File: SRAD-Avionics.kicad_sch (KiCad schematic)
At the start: 3 parts, among them J1 Conn_01x02_Socket, U2 STM32H503RBTx, U3 MAX-8C

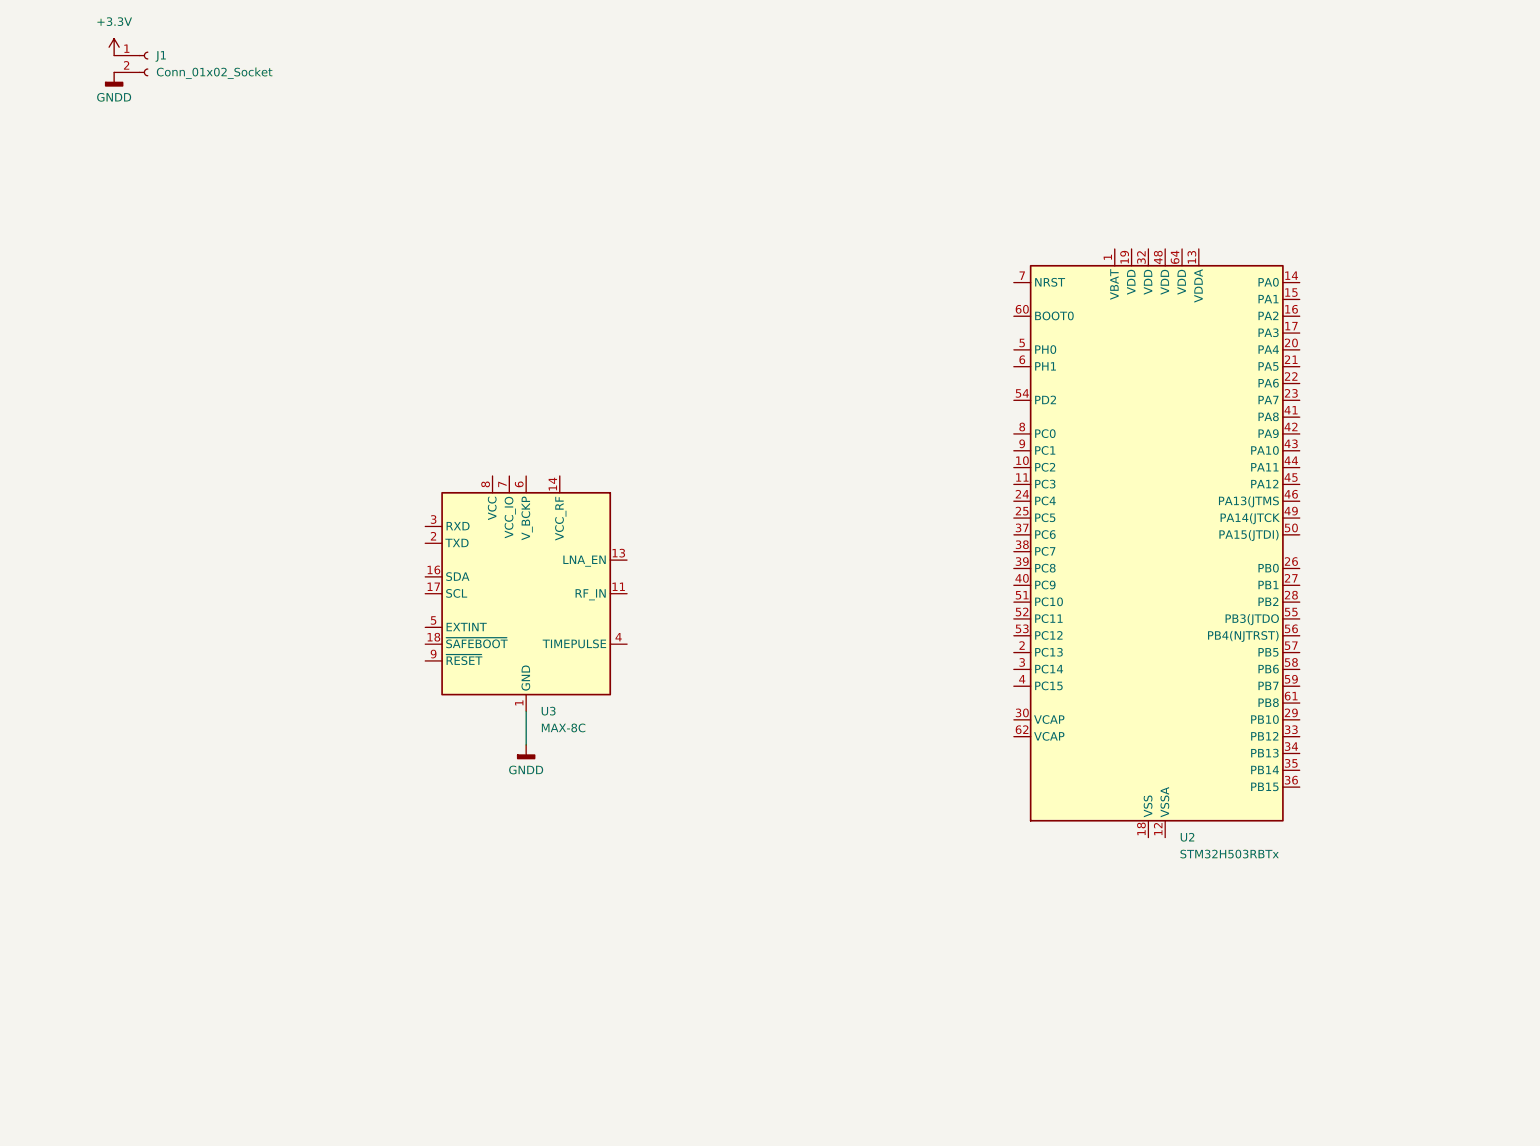
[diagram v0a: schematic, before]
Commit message: Finished schematics for battery charging and output voltage regulation
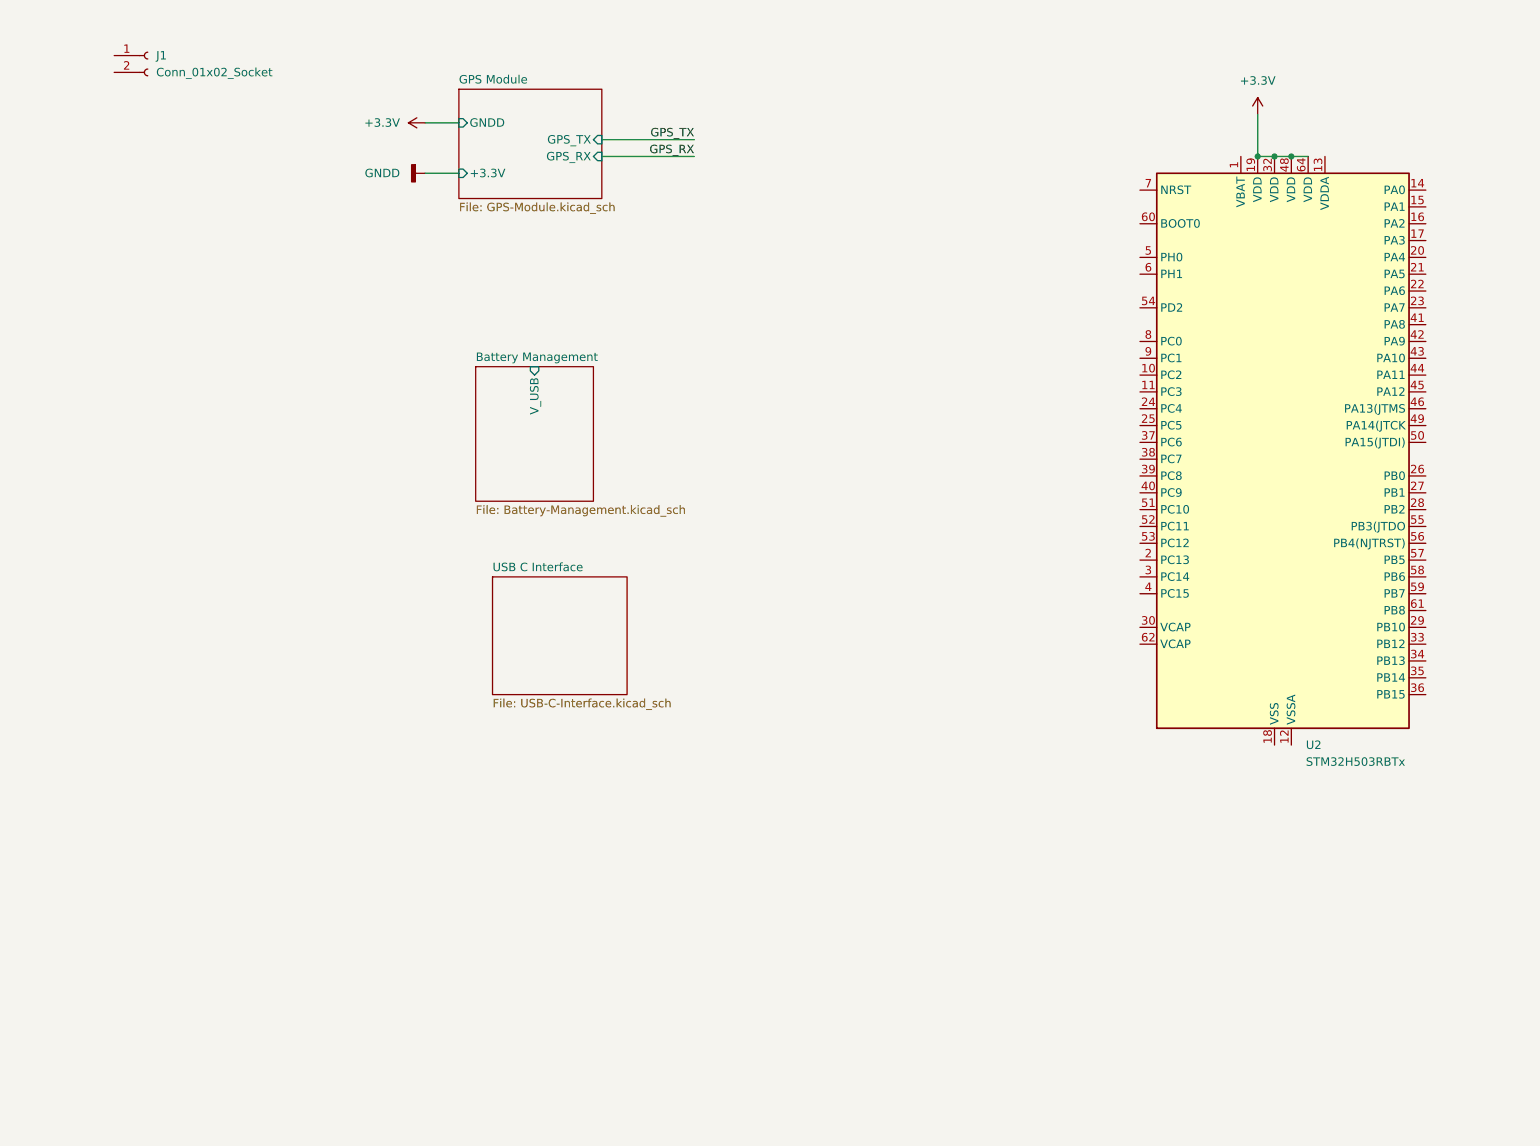
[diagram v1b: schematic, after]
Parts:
- removed U3: MAX-8C, RF_GPS:ublox_MAX, symbol RF_GPS:MAX-8C
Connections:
- net +3.3V: now also U2.19 (VDD), U2.32 (VDD), U2.48 (VDD), U2.64 (VDD); no longer J1.1 (Pin_1)
- net GNDD: no longer J1.2 (Pin_2)
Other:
- added sheet Battery Management (Battery-Management.kicad_sch)
- added sheet GPS Module (GPS-Module.kicad_sch)
- added sheet USB C Interface (USB-C-Interface.kicad_sch)
- moved on the sheet: U2

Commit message: Added USB C and CAN interfaces to schematic
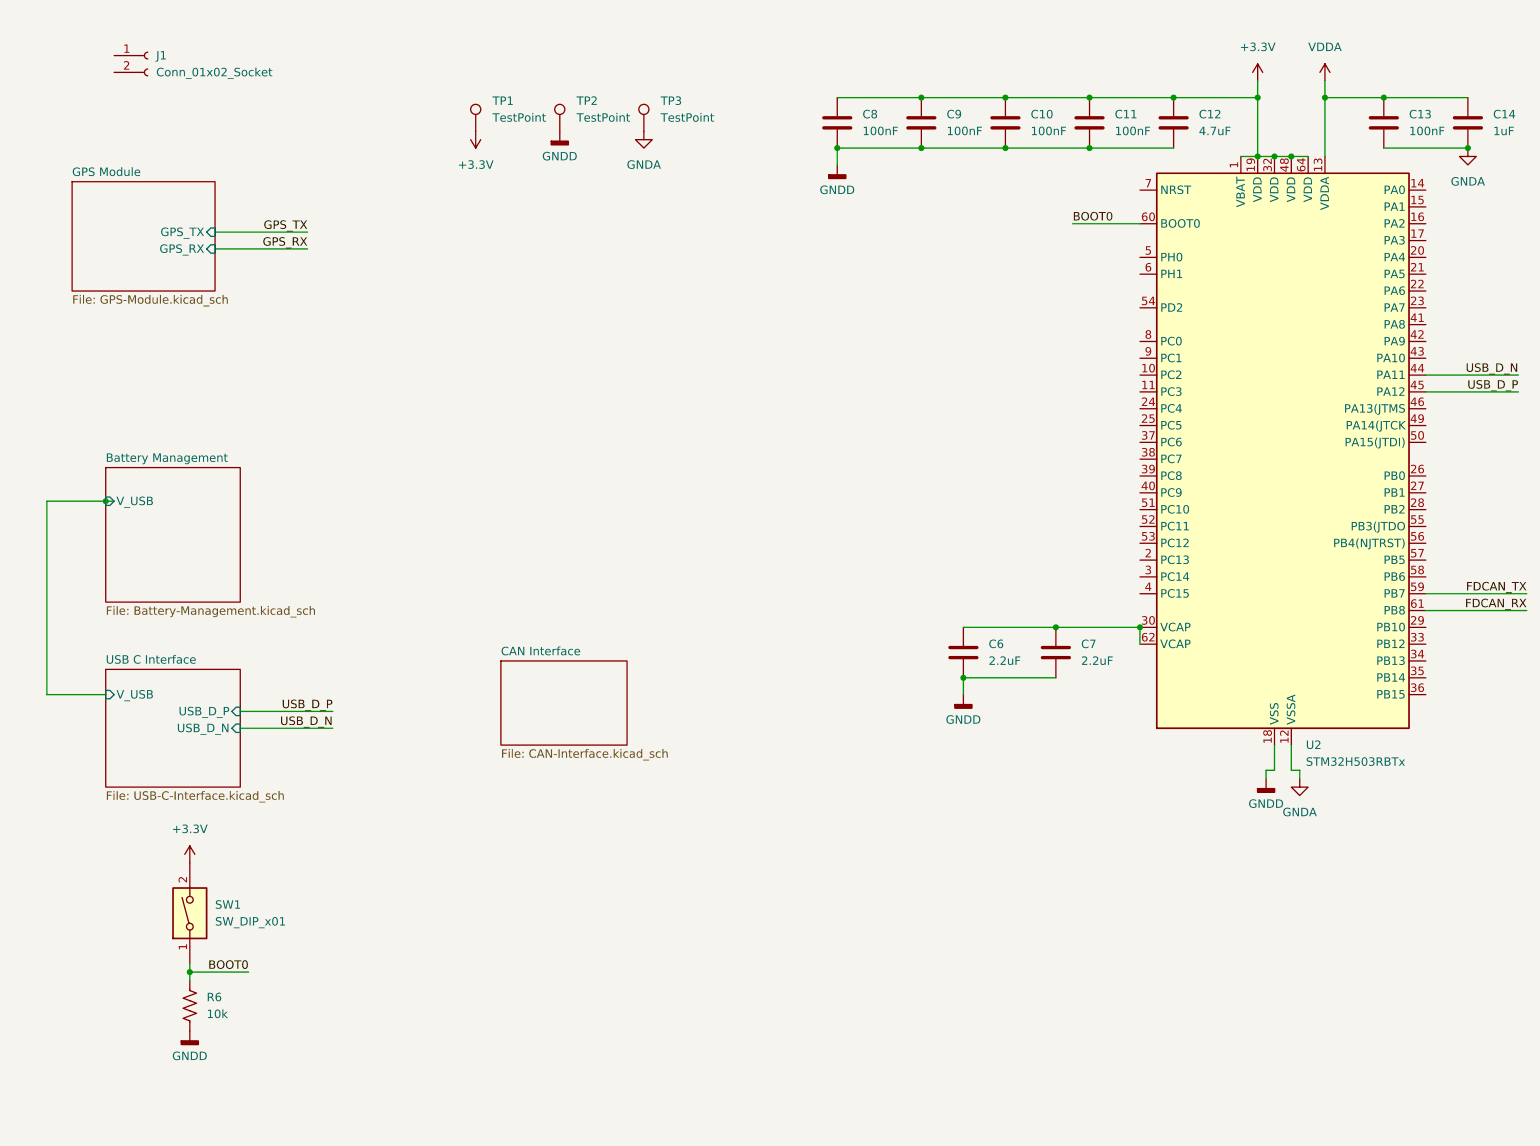
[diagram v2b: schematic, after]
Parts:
- added C10, C11, C13, C8, C9: 100nF, Capacitor_SMD:C_0603_1608Metric_Pad1.08x0.95mm_HandSolder, symbol Device:C
- added C12: 4.7uF, Capacitor_SMD:C_0603_1608Metric_Pad1.08x0.95mm_HandSolder, symbol Device:C
- added C14: 1uF, symbol Device:C
- added C6, C7: 2.2uF, Capacitor_SMD:C_0603_1608Metric_Pad1.08x0.95mm_HandSolder, symbol Device:C
- added R6: 10k, Resistor_SMD:R_0603_1608Metric_Pad0.98x0.95mm_HandSolder, symbol Device:R_US
- added SW1: SW_DIP_x01, symbol Switch:SW_DIP_x01
- added TP1, TP2, TP3: TestPoint, symbol Connector:TestPoint
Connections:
- net +3.3V: now also U2.1 (VBAT), C10.1, C11.1, C12.1, C8.1, C9.1, SW1.2, TP1.1
- net GNDD: now also U2.18 (VSS), U2.31 (VSS), U2.47 (VSS), U2.63 (VSS), C10.2, C11.2, C12.2, C6.2, C7.2, C8.2, C9.2, R6.2, TP2.1
- net GNDA: now reaches U2.12 (VSSA)
- net GNDA: now also C13.2, C14.2, TP3.1
- net VDDA: now reaches U2.13 (VDDA)
- net VDDA: now also C13.1, C14.1
- net at U2.30 (VCAP): now also U2.62 (VCAP), C6.1, C7.1
- net USB_D_N: now reaches U2.44 (PA11)
- net USB_D_P: now reaches U2.45 (PA12)
- net FDCAN_TX: now reaches U2.59 (PB7)
- net BOOT0: now reaches U2.60 (BOOT0)
- net BOOT0: now also R6.1, SW1.1
- net FDCAN_RX: now reaches U2.61 (PB8)
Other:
- added sheet CAN Interface (CAN-Interface.kicad_sch)
- sheet GPS Module ports: added none; removed +3.3V, GNDD
- sheet USB C Interface ports: added USB_D_N, USB_D_P, V_USB; removed none

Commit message: New, simpler CAN interface that supports FD CAN
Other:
- sheet CAN Interface ports: added FDCAN_RX, FDCAN_TX; removed none

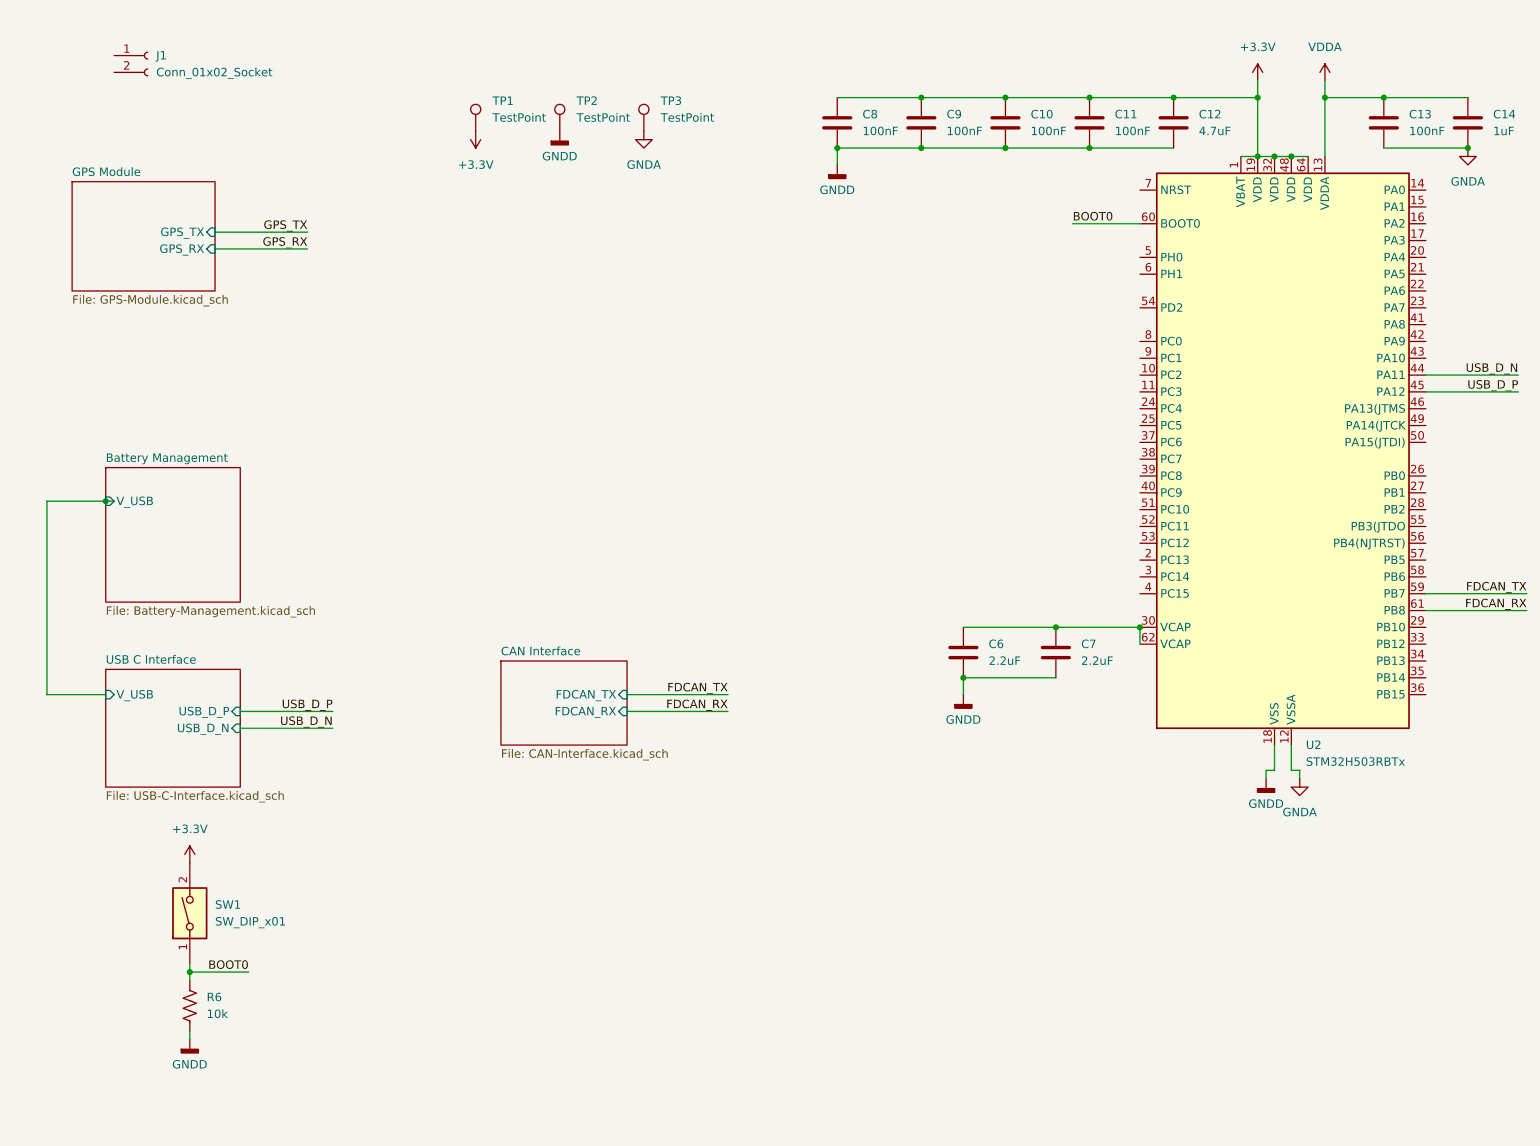
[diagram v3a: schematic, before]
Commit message: Routed USB interface from port to MCU and CAN interface from connector to transceiver
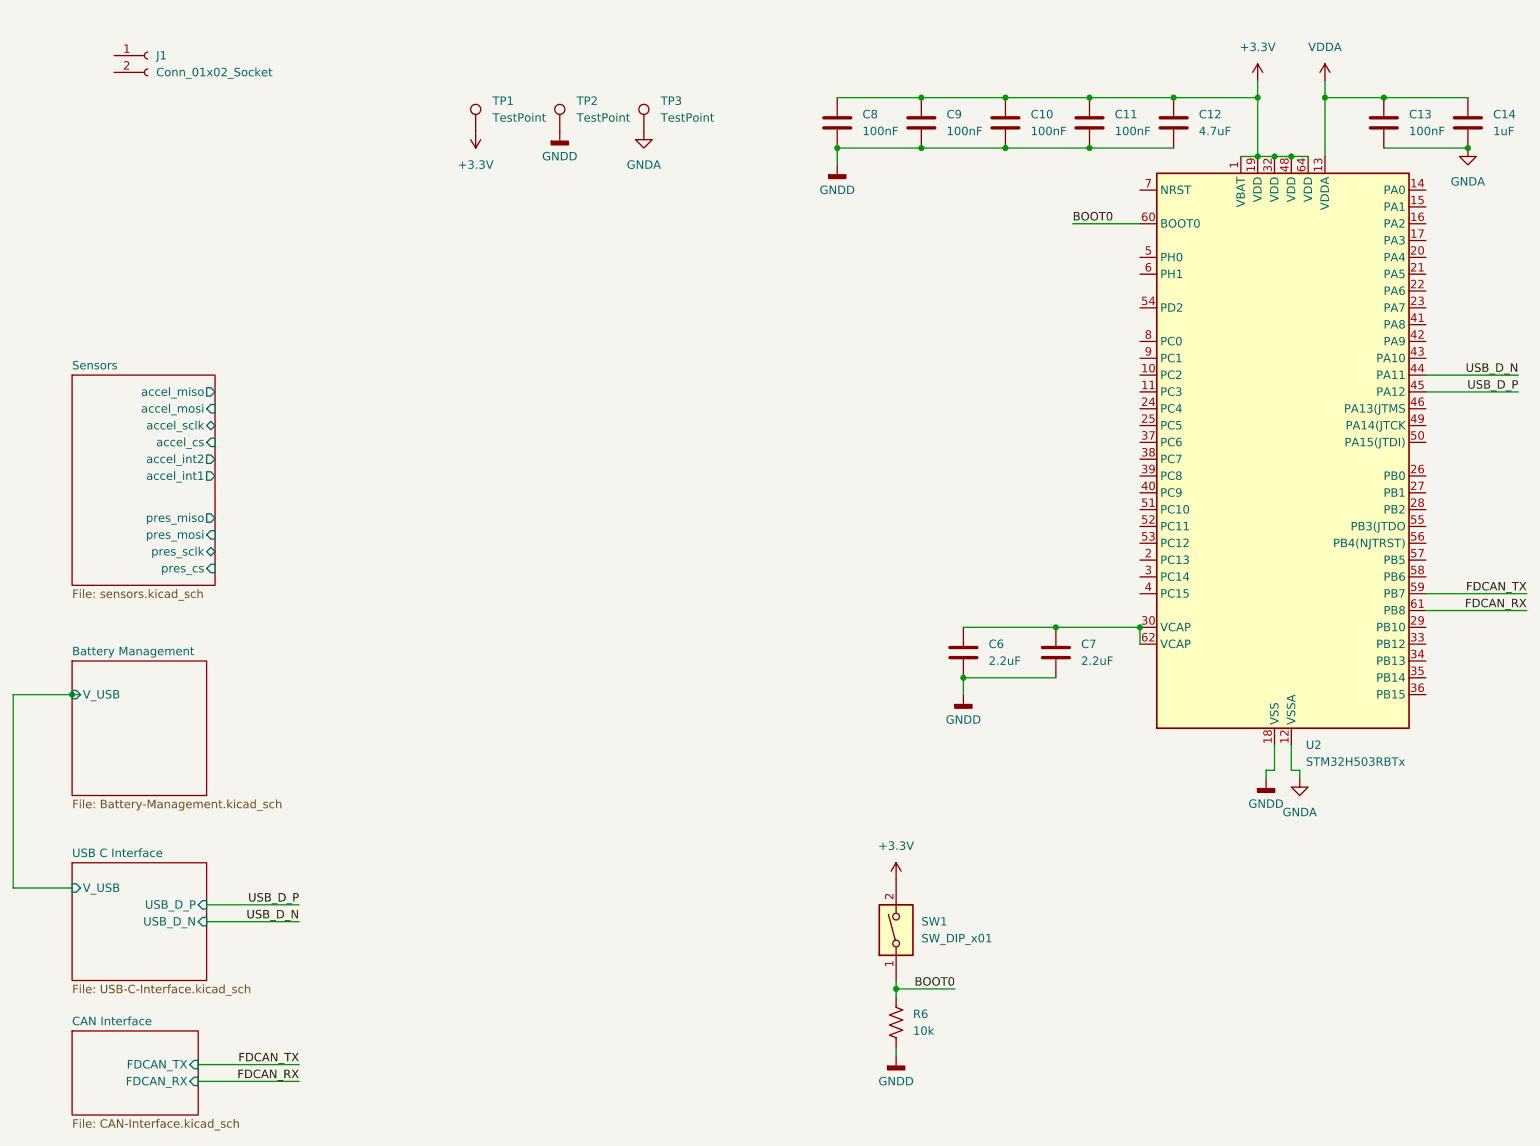
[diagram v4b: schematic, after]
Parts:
- C14: footprint (none) -> Capacitor_SMD:C_0603_1608Metric_Pad1.08x0.95mm_HandSolder
- SW1: footprint (none) -> Button_Switch_SMD:SW_DIP_SPSTx01_Slide_Copal_CHS-01B_W7.62mm_P1.27mm
- TP1, TP2, TP3: footprint (none) -> TestPoint:TestPoint_Loop_D2.60mm_Drill1.6mm_Beaded
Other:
- removed sheet GPS Module
- added sheet Sensors (sensors.kicad_sch)
- moved on the sheet: R6, SW1
